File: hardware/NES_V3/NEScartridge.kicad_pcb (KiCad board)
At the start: 4 copper layers, 39 parts, among them J1 Conn_02x36_Top_Bottom, U1 TXS0108EPW, U10 TXS0108EPW, U11 TXS0108EPW, U2 TXS0108EPW, U5 TXS0108EPW, U6 TXS0108EPW, U7 TXS0108EPW, U8 TXS0108EPW, U9 TXS0108EPW

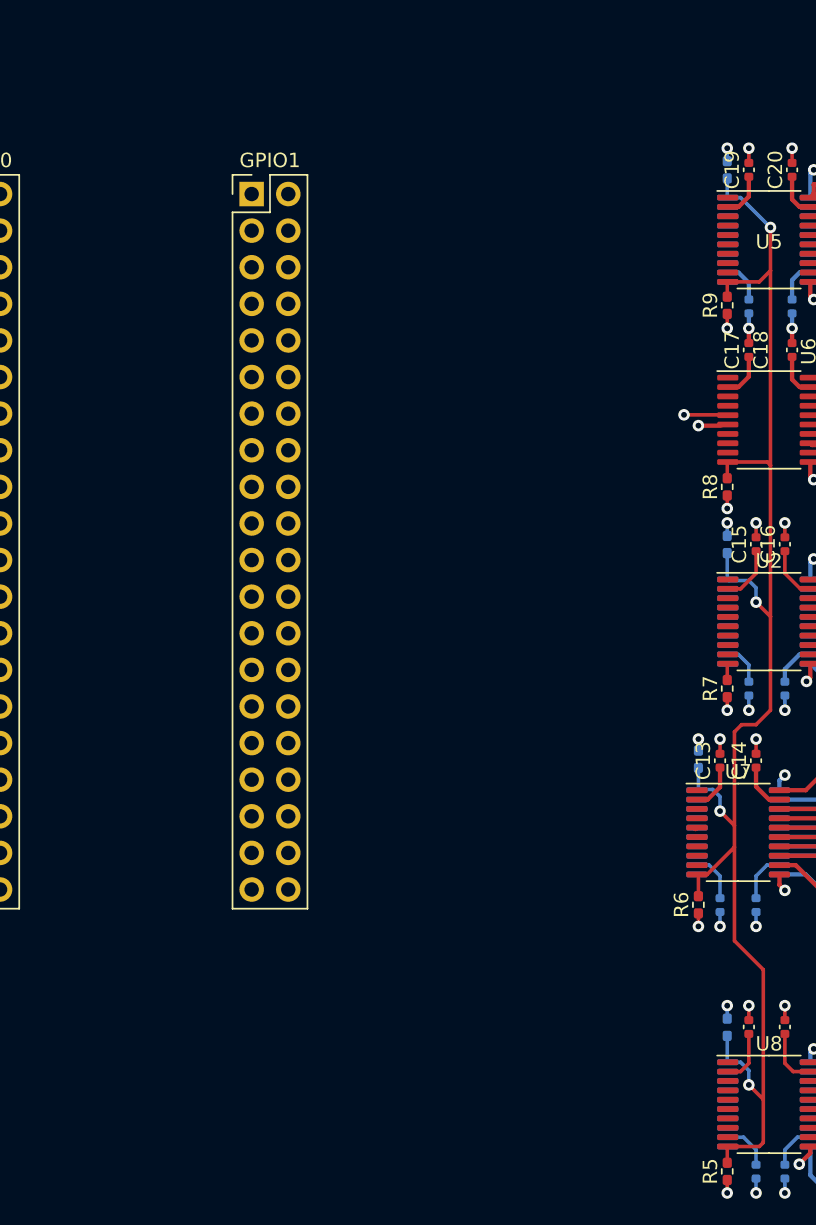
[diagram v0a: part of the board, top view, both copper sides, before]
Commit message: Update on the V3 of the cartridge
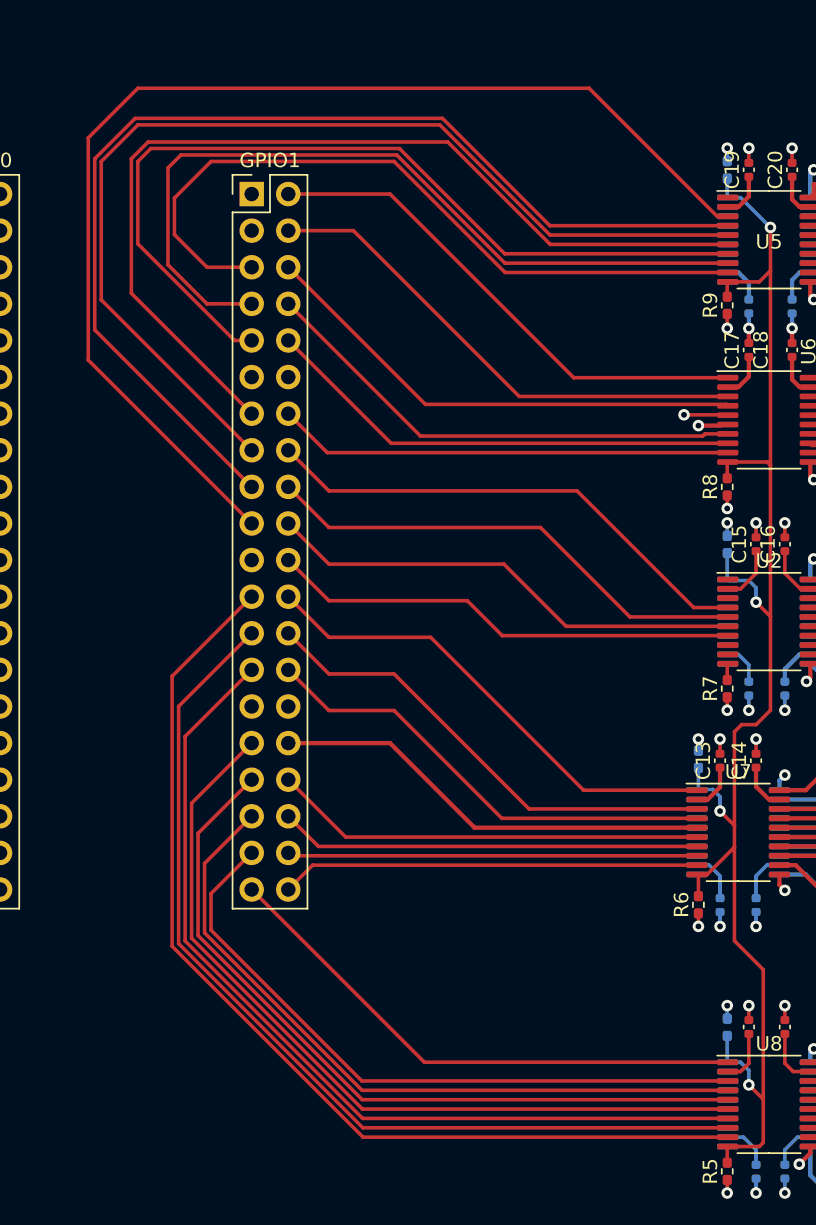
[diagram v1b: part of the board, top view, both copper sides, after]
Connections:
- GPIO1 pad 10: unconnected-(GPIO1-Pin_10-Pad10) -> (60C)PPUA8
- GPIO1 pad 13: unconnected-(GPIO1-Pin_13-Pad13) -> (29C)PPUA0
- GPIO1 pad 14: unconnected-(GPIO1-Pin_14-Pad14) -> (61C)PPUA9
- GPIO1 pad 15: unconnected-(GPIO1-Pin_15-Pad15) -> (33C)PPUD3
- GPIO1 pad 16: unconnected-(GPIO1-Pin_16-Pad16) -> (21C)PPU/RD
- GPIO1 pad 17: unconnected-(GPIO1-Pin_17-Pad17) -> (32C)PPUD2
- GPIO1 pad 18: unconnected-(GPIO1-Pin_18-Pad18) -> (20C)EXP4
- GPIO1 pad 19: unconnected-(GPIO1-Pin_19-Pad19) -> (31C)PPUD1
- GPIO1 pad 2: unconnected-(GPIO1-Pin_2-Pad2) -> (25C)PPUA4
- GPIO1 pad 20: unconnected-(GPIO1-Pin_20-Pad20) -> (19C)EXP3
- GPIO1 pad 21: unconnected-(GPIO1-Pin_21-Pad21) -> (30C)PPUD0
- GPIO1 pad 22: unconnected-(GPIO1-Pin_22-Pad22) -> (18C)EXP2
- GPIO1 pad 23: unconnected-(GPIO1-Pin_23-Pad23) -> (2C)CPUA11
- GPIO1 pad 24: unconnected-(GPIO1-Pin_24-Pad24) -> (17C)EXP1
- GPIO1 pad 25: unconnected-(GPIO1-Pin_25-Pad25) -> (3C)CPUA10
- GPIO1 pad 26: unconnected-(GPIO1-Pin_26-Pad26) -> (16C)EXP0
- GPIO1 pad 27: unconnected-(GPIO1-Pin_27-Pad27) -> (4C)CPUA9
- GPIO1 pad 28: unconnected-(GPIO1-Pin_28-Pad28) -> (15C)/IRQ
- GPIO1 pad 31: unconnected-(GPIO1-Pin_31-Pad31) -> (5C)CPUA8
- GPIO1 pad 32: unconnected-(GPIO1-Pin_32-Pad32) -> (14C)CPU.R/W
- GPIO1 pad 33: unconnected-(GPIO1-Pin_33-Pad33) -> (6C)CPUA7
- GPIO1 pad 34: unconnected-(GPIO1-Pin_34-Pad34) -> (13C)CPUA0
- GPIO1 pad 35: unconnected-(GPIO1-Pin_35-Pad35) -> (7C)CPUA6
- GPIO1 pad 36: unconnected-(GPIO1-Pin_36-Pad36) -> (12C)CPUA1
- GPIO1 pad 37: unconnected-(GPIO1-Pin_37-Pad37) -> (8C)CPUA5
- GPIO1 pad 38: unconnected-(GPIO1-Pin_38-Pad38) -> (11C)CPUA2
- GPIO1 pad 39: unconnected-(GPIO1-Pin_39-Pad39) -> (9C)CPUA4
- GPIO1 pad 4: unconnected-(GPIO1-Pin_4-Pad4) -> (24C)PPUA5
- GPIO1 pad 40: unconnected-(GPIO1-Pin_40-Pad40) -> (10C)CPUA3
- GPIO1 pad 5: unconnected-(GPIO1-Pin_5-Pad5) -> (26C)PPUA3
- GPIO1 pad 6: unconnected-(GPIO1-Pin_6-Pad6) -> (23C)PPUA6
- GPIO1 pad 7: unconnected-(GPIO1-Pin_7-Pad7) -> (27C)PPUA2
- GPIO1 pad 8: unconnected-(GPIO1-Pin_8-Pad8) -> (59C)PPUA7
- GPIO1 pad 9: unconnected-(GPIO1-Pin_9-Pad9) -> (28C)PPUA1
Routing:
- net (31C)PPUD1: track 0.00 -> 80.9 mm
- net (32C)PPUD2: track 0.00 -> 75.4 mm
- net (33C)PPUD3: track 0.00 -> 72.1 mm
- net (2C)CPUA11: track 0.00 -> 70.6 mm
- net (3C)CPUA10: track 0.00 -> 67.0 mm
- net (29C)PPUA0: track 0.00 -> 66.0 mm
- net (4C)CPUA9: track 0.00 -> 63.5 mm
- net (28C)PPUA1: track 0.00 -> 60.7 mm
- net (5C)CPUA8: track 0.00 -> 57.4 mm
- net (27C)PPUA2: track 0.00 -> 56.0 mm
- net (6C)CPUA7: track 0.00 -> 53.8 mm
- net (26C)PPUA3: track 0.00 -> 51.5 mm
- net (7C)CPUA6: track 0.00 -> 50.3 mm
- net (8C)CPUA5: track 0.00 -> 46.7 mm
- net (9C)CPUA4: track 0.00 -> 38.0 mm
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
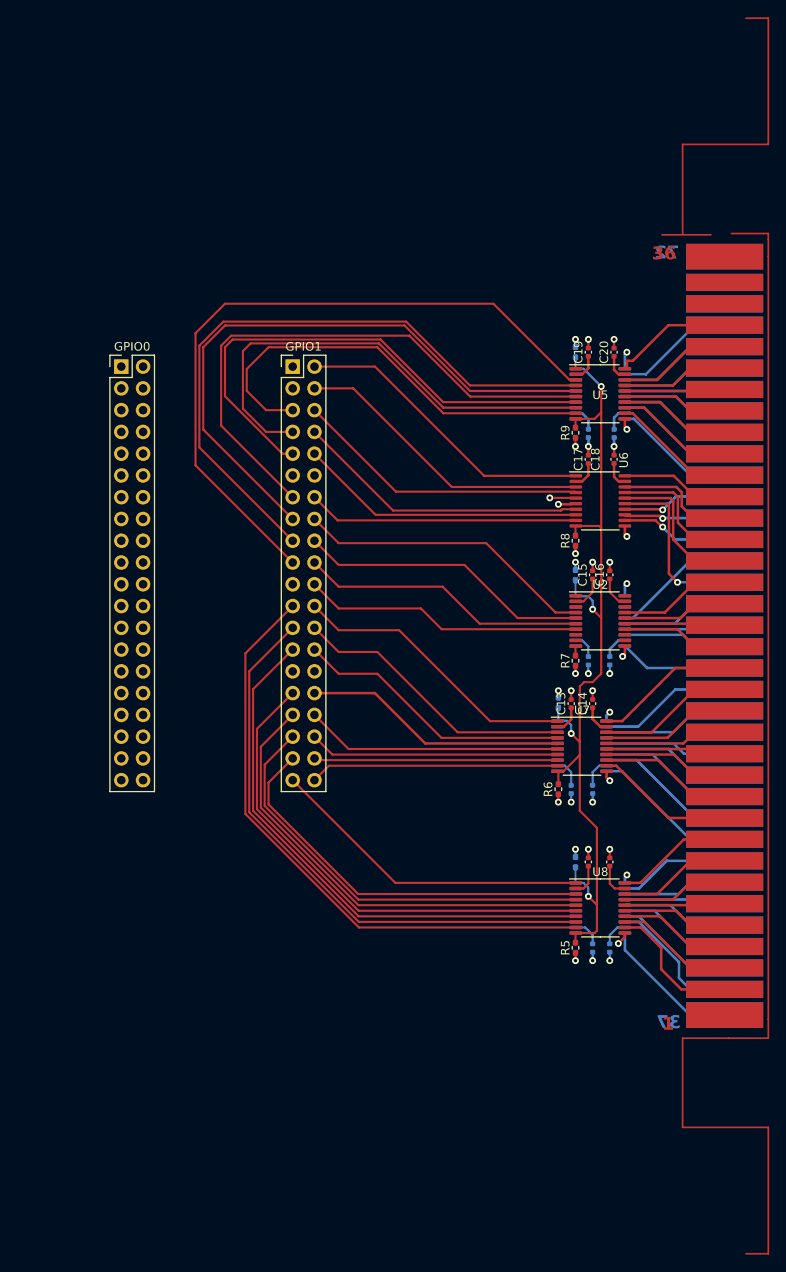
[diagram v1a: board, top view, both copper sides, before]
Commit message: Update on the V3 of the cartridge - PCB
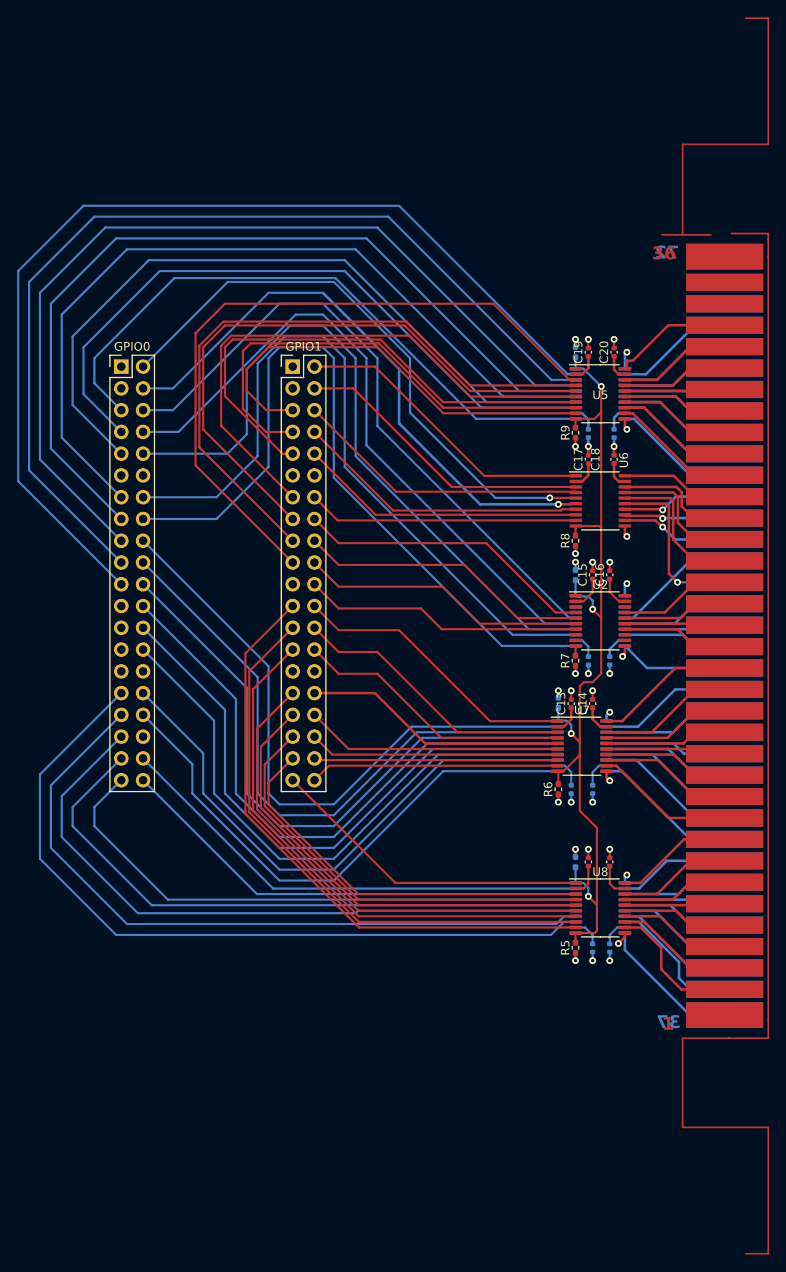
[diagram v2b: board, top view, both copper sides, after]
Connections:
- GPIO0 pad 10: (45C)CPUD4 -> (55C)EXP5
- GPIO0 pad 13: (13C)CPUA0 -> (65C)PPUA13
- GPIO0 pad 14: (44C)CPUD5 -> (54C)EXP6
- GPIO0 pad 15: (8C)CPUA5 -> (66C)PPUD7
- GPIO0 pad 16: (43C)CPUD6 -> (53C)EXP7
- GPIO0 pad 17: (7C)CPUA6 -> (67C)PPUD6
- GPIO0 pad 18: (42C)CPUD7 -> (52C)EXP8
- GPIO0 pad 19: (6C)CPUA7 -> (68C)PPUD5
- GPIO0 pad 2: (49C)CPUD0 -> (22C)CIRAMA10
- GPIO0 pad 20: (14C)CPU.R/W -> (51C)EXP9
- GPIO0 pad 21: (5C)CPUA8 -> (69C)PPUD4
- GPIO0 pad 22: (15C)/IRQ -> (50C)/ROMSEL (/A15 + /M2)
- GPIO0 pad 23: (4C)CPUA9 -> unconnected-(GPIO0-Pin_23-Pad23)
- GPIO0 pad 24: (57C)CIRAM/CE -> (49C)CPUD0
- GPIO0 pad 25: (3C)CPUA10 -> unconnected-(GPIO0-Pin_25-Pad25)
- GPIO0 pad 26: (22C)CIRAMA10 -> (48C)CPUD1
- GPIO0 pad 27: (2C)CPUA11 -> unconnected-(GPIO0-Pin_27-Pad27)
- GPIO0 pad 28: unconnected-(GPIO0-Pin_28-Pad28) -> (47C)CPUD2
- GPIO0 pad 3: (12C)CPUA1 -> unconnected-(GPIO0-Pin_3-Pad3)
- GPIO0 pad 31: (39C)CPUA12 -> (38C)M2
- GPIO0 pad 32: unconnected-(GPIO0-Pin_32-Pad32) -> (46C)CPUD3
- GPIO0 pad 33: (40C)CPUA13 -> (41C)CPUA14
- GPIO0 pad 34: unconnected-(GPIO0-Pin_34-Pad34) -> (45C)CPUD4
- GPIO0 pad 35: (41C)CPUA14 -> (40C)CPUA13
- GPIO0 pad 37: (38C)M2 -> (39C)CPUA12
- GPIO0 pad 38: unconnected-(GPIO0-Pin_38-Pad38) -> (44C)CPUD5
- GPIO0 pad 39: (50C)/ROMSEL (/A15 + /M2) -> (42C)CPUD7
- GPIO0 pad 4: (48C)CPUD1 -> (57C)CIRAM/CE
- GPIO0 pad 40: unconnected-(GPIO0-Pin_40-Pad40) -> (43C)CPUD6
- GPIO0 pad 5: (11C)CPUA2 -> (62C)PPUA11
- GPIO0 pad 6: (47C)CPUD2 -> (58C)PPU/A13
- GPIO0 pad 7: (10C)CPUA3 -> (63C)PPUA10
- GPIO0 pad 8: (46C)CPUD3 -> (56C)PPU/RD
- GPIO0 pad 9: (9C)CPUA4 -> (64C)PPUA12
- U6 pad 5: unconnected-(U6-A4-Pad5) -> (22C)CIRAMA10
- U6 pad 6: unconnected-(U6-A5-Pad6) -> (57C)CIRAM/CE
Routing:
- net (69C)PPUD4: track 0.00 -> 117.9 mm
- net (68C)PPUD5: track 0.00 -> 112.0 mm
- net (67C)PPUD6: track 0.00 -> 106.2 mm
- net (66C)PPUD7: track 0.00 -> 100.3 mm
- net (65C)PPUA13: track 0.00 -> 94.5 mm
- net (38C)M2: track 0.00 -> 90.1 mm
- net (53C)EXP7: track 0.00 -> 88.9 mm
- net (54C)EXP6: track 0.00 -> 86.5 mm
- net (64C)PPUA12: track 0.00 -> 85.3 mm
- net (41C)CPUA14: track 0.00 -> 84.2 mm
- net (55C)EXP5: track 0.00 -> 82.5 mm
- net (63C)PPUA10: track 0.00 -> 79.4 mm
- net (40C)CPUA13: track 0.00 -> 78.4 mm
- net (56C)PPU/RD: track 0.00 -> 77.1 mm
- net (58C)PPU/A13: track 0.00 -> 75.5 mm
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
